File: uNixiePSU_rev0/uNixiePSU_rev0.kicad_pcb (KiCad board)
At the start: 4 copper layers, 25 x 22 mm, 25 parts, among them J1 Conn_01x03, J2 Conn_01x02

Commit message: Update readme, add images
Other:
- board text added: "r0"
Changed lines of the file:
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@@
 			(at 0 0 0)
 			(layer "F.SilkS")
+			(hide yes)
 			(effects
 				(font
@@
 			(at 0 0 0)
 			(layer "F.SilkS")
+			(hide yes)
 			(effects
 				(font
@@
 		(layer "Edge.Cuts")
 	)
+	(gr_text "r0"
+		(at 18.15 9.65 -0)
+		(layer "B.SilkS")
+		(effects
+			(font
+				(size 1 1)
+				(thickness 0.15)
+			)
+			(justify mirror)
+		)
+	)
 	(gr_text "µNixiePSU"

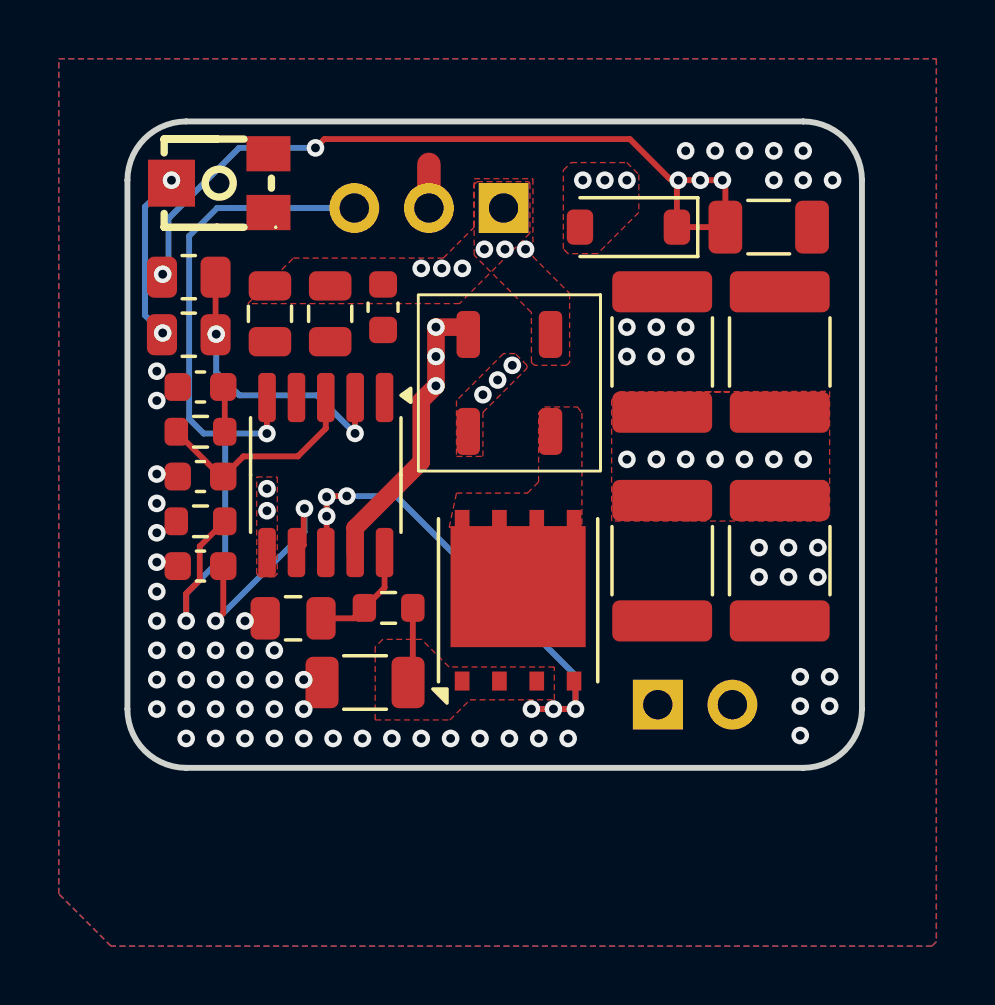
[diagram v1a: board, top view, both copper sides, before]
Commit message: Cleanup rev0 schematic
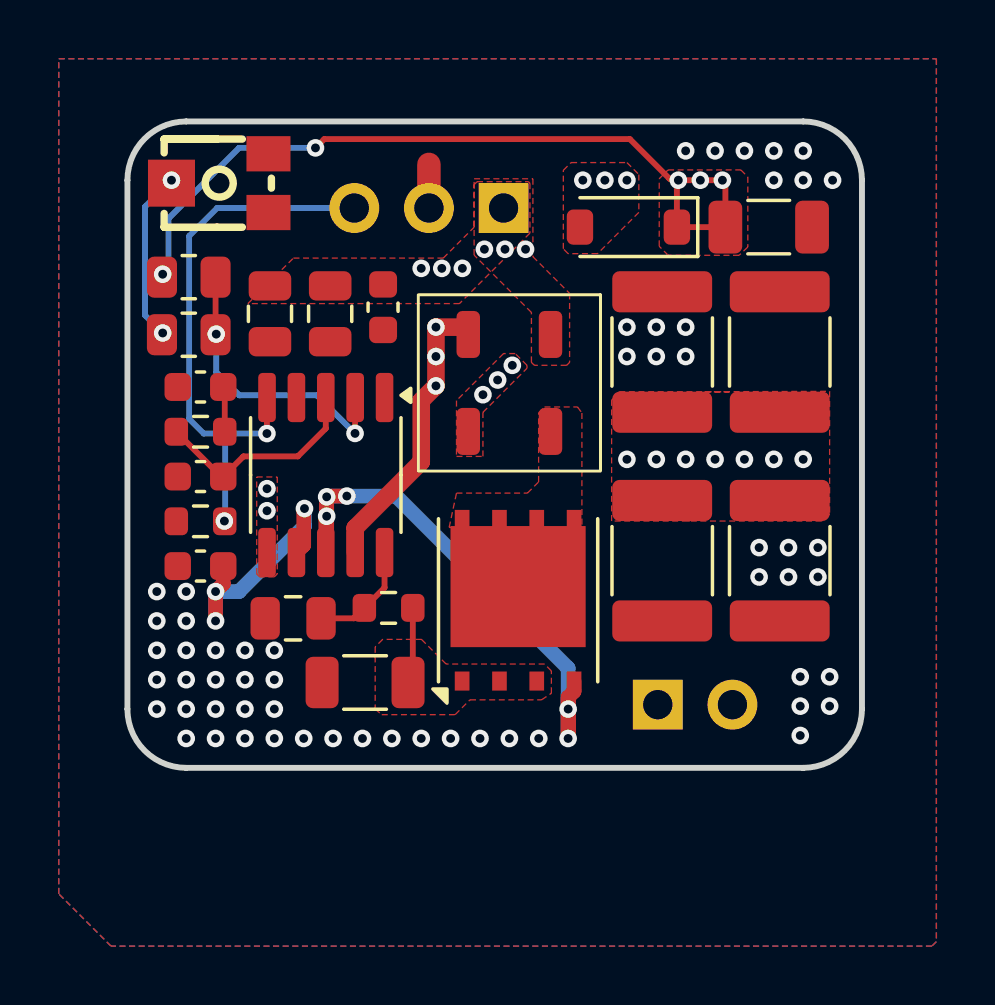
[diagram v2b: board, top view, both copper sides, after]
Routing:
- net /HV_SHDN: track 27.2 -> 19.4 mm
- net Net-(U1-G): track 19.8 -> 23.6 mm, vias 6 -> 5
- net Net-(U2-VCC): track 8.67 -> 9.13 mm, vias 2 -> 3
- net GND: vias 68 -> 60
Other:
- board text added: "Rev0"
- board text removed: "r0"
